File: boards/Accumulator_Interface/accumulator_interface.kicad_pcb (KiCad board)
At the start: 2 copper layers, 0 parts

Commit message: added traces to accumulator
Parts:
- added J1: INTERNAL, footprints:Ultrafit_4, B.Cu at (64.5, 64.0)
- added J10: AIR_CTRL_18, footprints:micromatch_female_vert_18, B.Cu at (37.8, 54.6)
- added J2: EXTERNAL, footprints:Ampseal_35, F.Cu at (115.3, 44.2)
- added J3: AIR_CTRL, footprints:Ultrafit_2, B.Cu at (113.3, 66.3)
- added J4: IMD_LATCH, footprints:Ultrafit_2, B.Cu at (102.9, 66.3)
- added J5: DISCHARGE, footprints:Ultrafit_2, B.Cu at (91.9, 66.3)
- added J6: BMS_Master, footprints:Ultrafit_4, B.Cu at (80.8, 64.0)
- added J7: BMS, footprints:micromatch_female_vert_12, B.Cu at (47.8, 85.9)
- added J8: TSAL/AIL, footprints:micromatch_female_vert_4, B.Cu at (45.7, 36.8)
- added J9: IMD_LATCH, footprints:micromatch_female_vert_4, B.Cu at (45.7, 50.0)
- added U1: RJ45_VT_AIR, footprints:RJ45-Vertical, F.Cu at (52.1, 67.8)
- added U2: RJ45_VT_BMS, footprints:RJ45-Vertical, F.Cu at (38.9, 100.3)
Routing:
- net /CAN_LOW: track 0.00 -> 194.2 mm
- net /BMS_IN/IMD_LATCH_OUT: track 0.00 -> 79.7 mm
- net /IMD_LATCH_IN/HVD_OUT: track 0.00 -> 74.1 mm
- net /CAN_HIGH: track 0.00 -> 46.5 mm, vias 0 -> 1
- net /HVD_IN/MAIN_PACK_OUT: track 0.00 -> 44.3 mm
- net /TSAL+: track 0.00 -> 27.1 mm
- net /SCK_AIR: track 0.00 -> 26.0 mm
- net /TSMS_IN: track 0.00 -> 24.3 mm
- net /MISO_AIR: track 0.00 -> 23.1 mm, vias 0 -> 1
- net /MOSI_AIR: track 0.00 -> 22.4 mm
- net /AIR_CTRL_LED_1: track 0.00 -> 21.1 mm
- net /AIR_CTRL_5V_OUT: track 0.00 -> 20.2 mm
- net /BMS_LED_2: track 0.00 -> 17.8 mm, vias 0 -> 1
- net /TSAL-: track 0.00 -> 17.6 mm
- net /IMD_LATCH_STATUS: track 0.00 -> 16.9 mm, vias 0 -> 2
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
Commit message: Accu Interface updates
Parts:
- added J11: Energy_Meter_Power, footprints:Ultrafit_2, B.Cu at (66.2, 77.0)
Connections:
- J10 pad 12: /BMS_IN/IMD_LATCH_OUT -> /BMS_STATUS
- J10 pad 13: /IMD_LATCH_IN/HVD_OUT -> /IMD_LATCH_STATUS
- J10 pad 14: /MAIN_PACK_IN/BMS_OUT -> /BMS_IN/IMD_LATCH_OUT
- J10 pad 15: /HVD_IN/MAIN_PACK_OUT -> /IMD_LATCH_IN/HVD_OUT
- J10 pad 16: /BMS_STATUS -> /MAIN_PACK_IN/BMS_OUT
- J10 pad 17: /IMD_LATCH_STATUS -> /HVD_IN/MAIN_PACK_OUT
- J10 pad 18: Net-(J10-Pad18) -> (no net)
- J2 pad 16: Net-(J2-Pad16) -> (no net)
- J2 pad 17: Net-(J2-Pad17) -> (no net)
- J2 pad 18: Net-(J2-Pad18) -> (no net)
- J2 pad 19: Net-(J2-Pad19) -> (no net)
- J2 pad 20: Net-(J2-Pad20) -> (no net)
- J2 pad 21: Net-(J2-Pad21) -> (no net)
- J2 pad 22: Net-(J2-Pad22) -> (no net)
- J2 pad 23: Net-(J2-Pad23) -> (no net)
- J2 pad 33: Net-(J2-Pad33) -> (no net)
- J3 pad 2: Net-(J3-Pad2) -> (no net)
- U1 pad 3: Net-(U1-Pad3) -> /AIR_CTRL_RESET
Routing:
- net /12V: track 0.00 -> 153.2 mm, vias 0 -> 8
- net /CAN_HIGH: track 46.5 -> 136.9 mm, vias 1 -> 3
- net /BSPD_CURRENT_SENSE: track 0.00 -> 84.3 mm, vias 0 -> 9
- net /CAN_LOW: track 194.2 -> 122.8 mm, vias 0 -> 4
- net /FAN_PWM: track 0.00 -> 62.6 mm, vias 0 -> 6
- net /BMS_STATUS: track 0.00 -> 46.2 mm, vias 0 -> 3
- net /CRASH_IN/HVD_OUT: track 11.0 -> 54.7 mm
- net /MAIN_PACK_IN/BMS_OUT: track 15.5 -> 56.5 mm, vias 0 -> 1
- net /AIR_CTRL_LED_2: track 0.00 -> 40.3 mm, vias 0 -> 1
- net /TSMS_IN: track 24.3 -> 62.0 mm, vias 0 -> 2
- net /BMS_LED_1: track 0.00 -> 29.3 mm, vias 0 -> 1
- net /AIR_CTRL_RESET: track 0.00 -> 27.1 mm, vias 0 -> 2
- net /GND: track 0.00 -> 8.00 mm
- net /FAN_GND: track 0.00 -> 8.00 mm
- net /FAN_12V: track 0.00 -> 8.00 mm
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- added copper zone on B.Cu, net /GND
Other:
- board text added: "12V"
- board text added: "BMS_OUT"
- board text added: "HVD_OUT"
- board text added: "IMD_LATCH_OUT"
- board text added: "MAIN_PACK_OUT"
- board text added: "TSMS_IN"

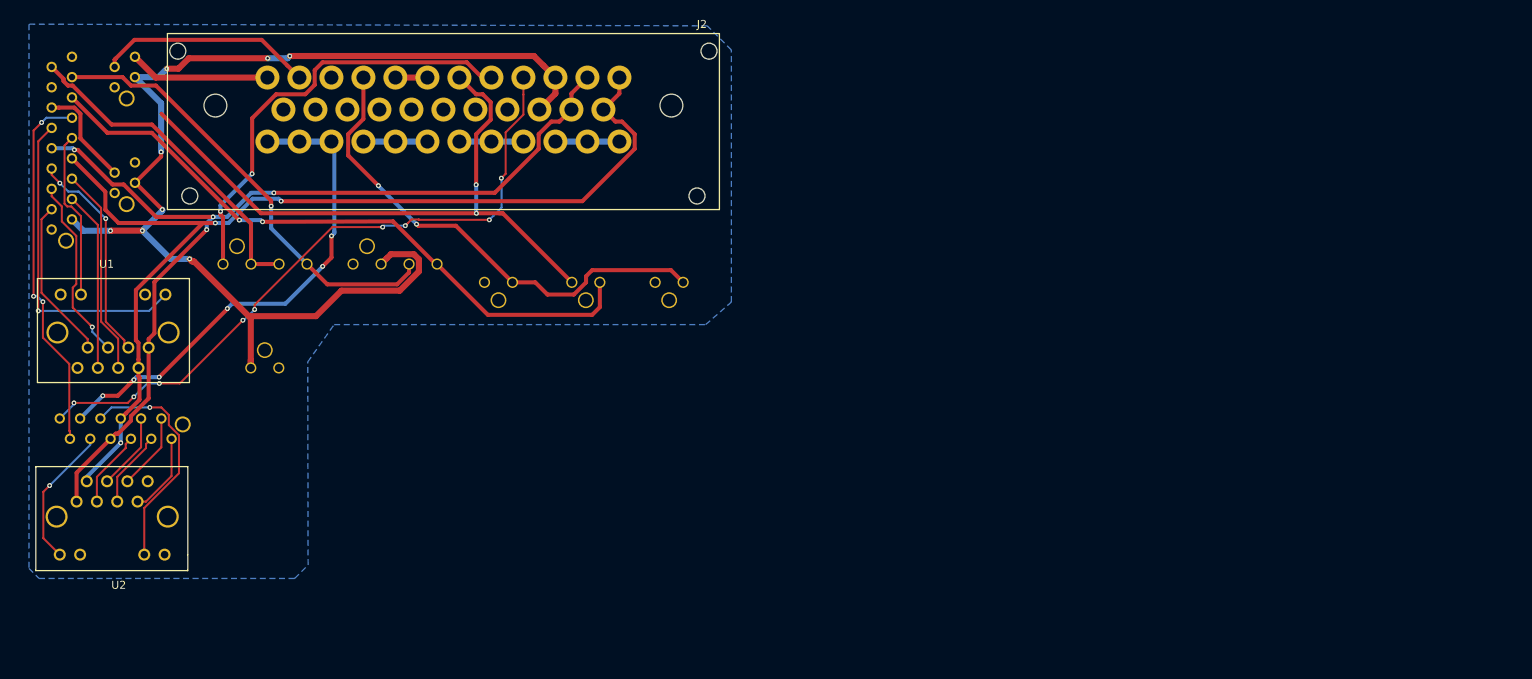
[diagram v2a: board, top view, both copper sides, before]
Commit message: Modified layout for accumulator board.
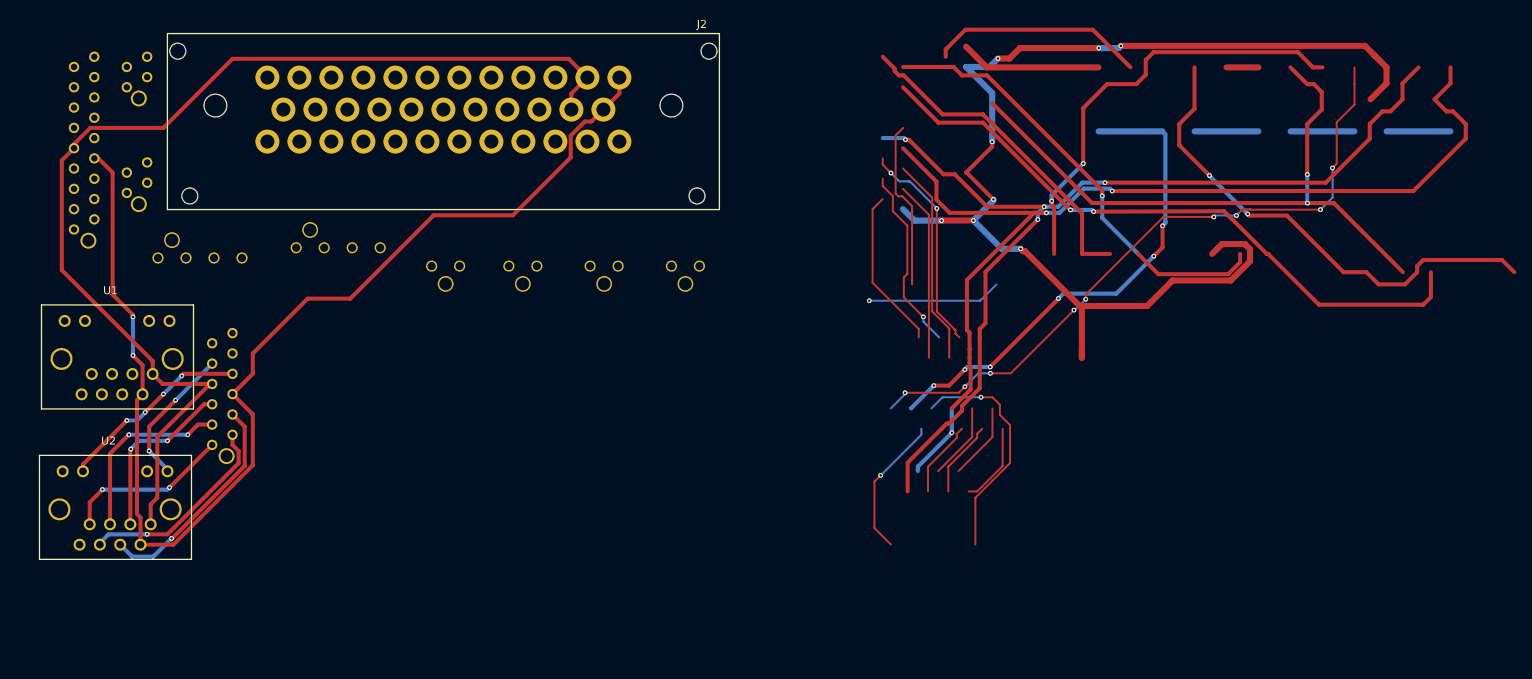
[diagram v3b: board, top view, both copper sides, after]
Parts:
- moved J11 31.4 mm to (95.0, 64.3), turned to 270 degrees
- moved U2 17.0 mm to (52.3, 89.9), turned to 180 degrees
- moved J7 11.0 mm to (57.9, 81.5), turned to 0 degrees
- moved J1 8.16 mm to (56.4, 63.2)
- moved J6 7.40 mm to (73.7, 62.0)
- moved J5 6.91 mm to (85.3, 64.3)
- moved U1 3.34 mm to (52.6, 71.1)
- moved J4 3.06 mm to (105.2, 64.3)
- moved J3 2.87 mm to (115.3, 64.3)
- moved J10 2.79 mm to (40.6, 54.6)
- moved J8 1.52 mm to (47.2, 36.8)
- moved J9 1.52 mm to (47.2, 50.0)
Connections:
- J10 pad 12: /BMS_STATUS -> /IMD_LATCH_STATUS
- J10 pad 13: /IMD_LATCH_STATUS -> /BMS_STATUS
- J10 pad 18: (no net) -> Net-(J10-Pad18)
- J2 pad 16: (no net) -> Net-(J2-Pad16)
- J2 pad 17: (no net) -> Net-(J2-Pad17)
- J2 pad 18: (no net) -> Net-(J2-Pad18)
- J2 pad 19: (no net) -> Net-(J2-Pad19)
- J2 pad 20: (no net) -> Net-(J2-Pad20)
- J2 pad 21: (no net) -> Net-(J2-Pad21)
- J2 pad 22: (no net) -> Net-(J2-Pad22)
- J2 pad 23: (no net) -> Net-(J2-Pad23)
- J2 pad 33: (no net) -> Net-(J2-Pad33)
- J3 pad 2: (no net) -> Net-(J3-Pad2)
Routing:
- net (no net): track 0.00 -> 1261.2 mm, vias 0 -> 45
- net /12V: track 153.2 -> 0.00 mm, vias 8 -> 0
- net /BSPD_CURRENT_SENSE: track 84.3 -> 0.00 mm, vias 9 -> 0
- net /BMS_IN/IMD_LATCH_OUT: track 80.8 -> 0.00 mm, vias 2 -> 0
- net /IMD_LATCH_IN/HVD_OUT: track 80.3 -> 0.00 mm, vias 2 -> 0
- net /FAN_PWM: track 62.6 -> 0.00 mm, vias 6 -> 0
- net /TSMS_IN: track 62.0 -> 0.00 mm, vias 2 -> 0
- net /MAIN_PACK_IN/BMS_OUT: track 56.5 -> 0.00 mm, vias 1 -> 0
- net /CRASH_IN/HVD_OUT: track 54.7 -> 0.00 mm, vias 2 -> 0
- net /BMS_STATUS: track 46.2 -> 0.00 mm, vias 3 -> 0
- net /HVD_IN/MAIN_PACK_OUT: track 41.8 -> 0.00 mm
- net /AIR_CTRL_LED_2: track 40.3 -> 0.00 mm, vias 1 -> 0
- net /TSAL+: track 27.2 -> 0.00 mm
- net /AIR_CTRL_RESET: track 27.1 -> 0.00 mm, vias 2 -> 0
- net /SCK_AIR: track 26.0 -> 0.00 mm
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- removed copper zone on B.Cu, net /GND

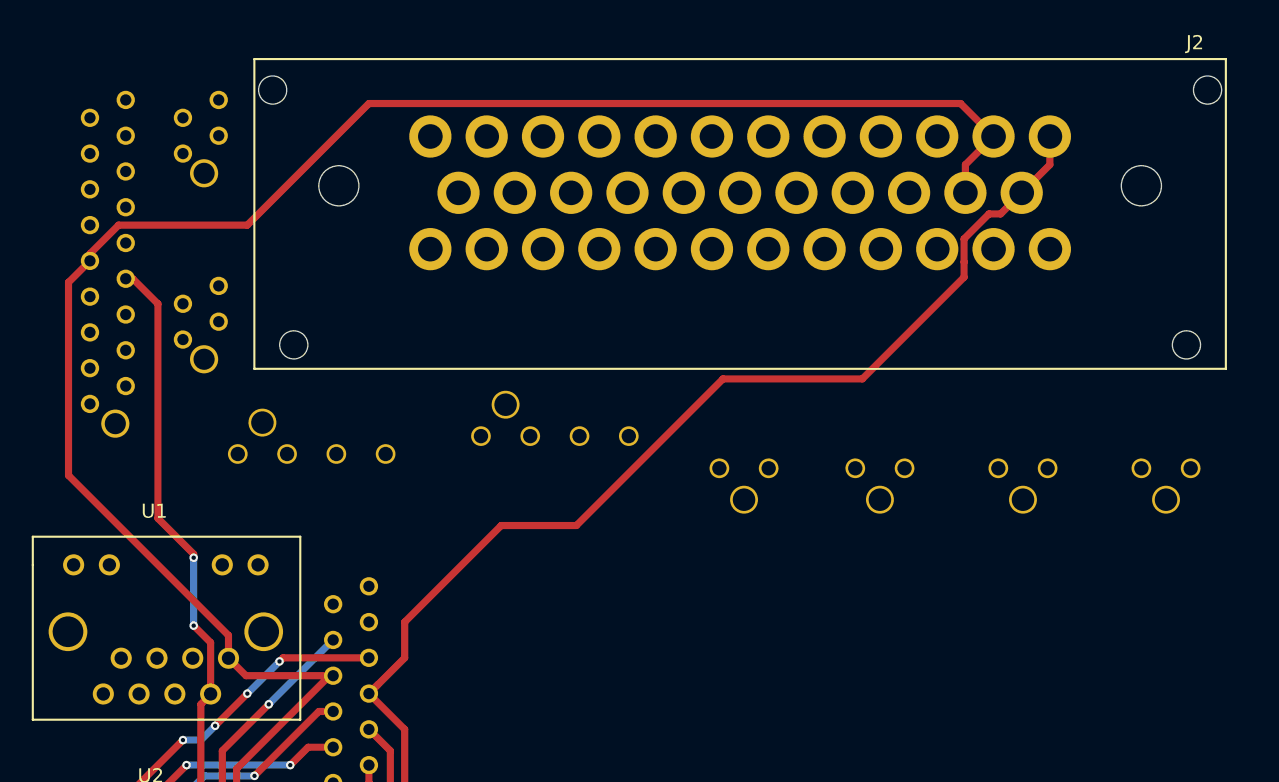
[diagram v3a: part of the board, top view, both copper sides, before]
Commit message: added more traces
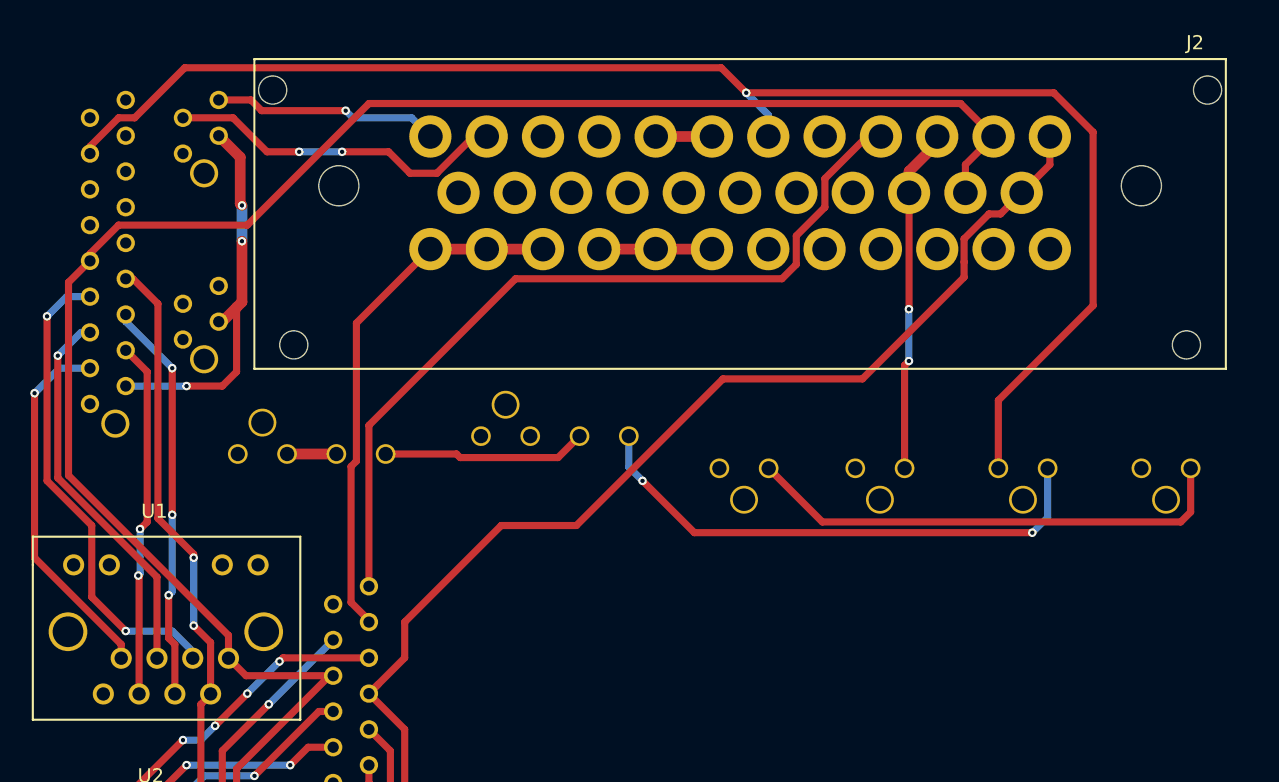
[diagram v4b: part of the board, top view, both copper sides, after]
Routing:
- net /IMD_LATCH_IN/HVD_OUT: track 0.00 -> 106.4 mm, vias 0 -> 1
- net /BSPD_CURRENT_SENSE: track 0.00 -> 58.7 mm
- net /12V: track 0.00 -> 52.1 mm, vias 0 -> 5
- net /BMS_IN/IMD_LATCH_OUT: track 0.00 -> 37.8 mm, vias 0 -> 2
- net /FAN_PWM: track 0.00 -> 37.3 mm
- net /TSMS_IN: track 0.00 -> 34.9 mm
- net /AIR_CTRL_RESET: track 0.00 -> 34.1 mm, vias 0 -> 2
- net /SCK_AIR: track 0.00 -> 28.6 mm, vias 0 -> 3
- net /MISO_AIR: track 0.00 -> 27.4 mm, vias 0 -> 1
- net /AIR_CTRL_5V_OUT: track 0.00 -> 26.0 mm, vias 0 -> 1
- net /TSAL+: track 0.00 -> 25.8 mm, vias 0 -> 2
- net /MOSI_AIR: track 0.00 -> 25.3 mm, vias 0 -> 2
- net /TSAL-: track 0.00 -> 16.1 mm, vias 0 -> 1
- net /MAIN_PACK_IN/BMS_OUT: track 0.00 -> 14.5 mm
- net /FAN_12V: track 0.00 -> 8.00 mm
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
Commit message: Accum Update
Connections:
- J10 pad 18: Net-(J10-Pad18) -> (no net)
- J2 pad 16: Net-(J2-Pad16) -> /12V
- J2 pad 17: Net-(J2-Pad17) -> /12V
- J2 pad 18: Net-(J2-Pad18) -> /CAN_LOW
- J2 pad 19: Net-(J2-Pad19) -> /CAN_LOW
- J2 pad 20: Net-(J2-Pad20) -> /CAN_HIGH
- J2 pad 21: Net-(J2-Pad21) -> /CAN_HIGH
- J2 pad 22: Net-(J2-Pad22) -> /GND
- J2 pad 23: Net-(J2-Pad23) -> /GND
- J2 pad 33: Net-(J2-Pad33) -> (no net)
- J2 pad 4: /FAN_GND -> /GND
- J2 pad 5: /FAN_GND -> /GND
- J2 pad 6: /FAN_GND -> /GND
- J2 pad 7: /FAN_12V -> /12V
- J2 pad 8: /FAN_12V -> /12V
- J2 pad 9: /FAN_12V -> /12V
- J3 pad 2: Net-(J3-Pad2) -> (no net)
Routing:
- net /12V: track 52.1 -> 162.7 mm, vias 5 -> 10
- net /CAN_HIGH: track 149.9 -> 219.0 mm, vias 2 -> 4
- net /CRASH_IN/HVD_OUT: track 0.00 -> 62.0 mm, vias 0 -> 5
- net /BMS_IN/IMD_LATCH_OUT: track 37.8 -> 82.8 mm, vias 2 -> 8
- net /HVD_IN/MAIN_PACK_OUT: track 3.50 -> 48.5 mm, vias 0 -> 4
- net /BMS_STATUS: track 0.00 -> 37.4 mm, vias 0 -> 2
- net /MAIN_PACK_IN/BMS_OUT: track 14.5 -> 47.0 mm, vias 0 -> 3
- net /AIR_CTRL_LED_2: track 0.00 -> 30.1 mm, vias 0 -> 3
- net /TSMS_IN: track 34.9 -> 64.6 mm, vias 0 -> 4
- net /AIR_CTRL_LED_1: track 0.00 -> 25.1 mm, vias 0 -> 1
- net /GND: track 0.00 -> 24.0 mm
- net /CAN_LOW: track 137.3 -> 154.5 mm, vias 0 -> 1
- net /IMD_LATCH_STATUS: track 0.00 -> 9.43 mm, vias 0 -> 1
- net /FAN_12V: track 8.00 -> 0.00 mm
- net /SCK_AIR: track 28.6 -> 30.3 mm, vias 3 -> 4
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- added copper zone on B.Cu, net /GND

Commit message: Accum Update
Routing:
- net /CAN_HIGH: track 219.0 -> 221.2 mm
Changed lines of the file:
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@@
   (general
     (links 83)
-    (no_connects 8)
+    (no_connects 0)
     (area 19.692111 25.50813 221.076402 105.306801)
     (thickness 1.6)
     (drawings 20)
-    (tracks 895)
+    (tracks 900)
     (zones 0)
     (modules 13)
@@
   )
   (setup
-    (last_trace_width 0.508)
+    (last_trace_width 0.762)
     (user_trace_width 0.254)
     (user_trace_width 0.508)
@@
   (segment (start 46.228 76.327) (end 46.228 73.279) (width 0.508) (layer F.Cu) (net 16))
   (segment (start 46.668 76.767) (end 46.228 76.327) (width 0.508) (layer F.Cu) (net 16))
-  (segment (start 78.816 44.696) (end 80.315999 46.195999) (width 0.508) (layer B.Cu) (net 17))
-  (segment (start 82.909599 47.968125) (end 82.909599 50.736923) (width 0.508) (layer B.Cu) (net 17))
-  (segment (start 80.315999 46.195999) (end 81.137473 46.195999) (width 0.508) (layer B.Cu) (net 17))
-  (segment (start 82.909599 50.736923) (end 87.595468 55.422792) (width 0.508) (layer B.Cu) (net 17))
-  (segment (start 81.137473 46.195999) (end 82.909599 47.968125) (width 0.508) (layer B.Cu) (net 17))
-  (segment (start 87.595468 55.422792) (end 87.900267 55.727591) (width 0.508) (layer B.Cu) (net 17))
-  (segment (start 74.816 44.696) (end 74.816 50.433054) (width 0.508) (layer B.Cu) (net 17))
-  (segment (start 74.816 50.433054) (end 80.110537 55.727591) (width 0.508) (layer B.Cu) (net 17))
-  (segment (start 80.110537 55.727591) (end 87.469215 55.727591) (width 0.508) (layer B.Cu) (net 17))
-  (segment (start 87.469215 55.727591) (end 87.900267 55.727591) (width 0.508) (layer B.Cu) (net 17))
+  (segment (start 74.816 47.92472) (end 74.816 49.75352) (width 0.508) (layer B.Cu) (net 17))
+  (segment (start 74.816 44.696) (end 74.816 47.92472) (width 0.762) (layer B.Cu) (net 17))
+  (segment (start 74.816 49.75352) (end 74.816 50.61266) (width 0.762) (layer B.Cu) (net 17))
+  (segment (start 74.816 50.61266) (end 79.930931 55.727591) (width 0.762) (layer B.Cu) (net 17))
+  (segment (start 87.469215 55.727591) (end 87.900267 55.727591) (width 0.762) (layer B.Cu) (net 17))
+  (segment (start 79.930931 55.727591) (end 87.469215 55.727591) (width 0.762) (layer B.Cu) (net 17))
+  (segment (start 82.849401 47.719967) (end 82.849401 49.672033) (width 0.508) (layer B.Cu) (net 17))
+  (segment (start 82.849401 49.672033) (end 82.782599 49.738835) (width 0.508) (layer B.Cu) (net 17))
+  (segment (start 82.849401 47.907927) (end 82.849401 47.719967) (width 0.762) (layer B.Cu) (net 17))
+  (segment (start 82.849401 47.719967) (end 81.325433 46.195999) (width 0.762) (layer B.Cu) (net 17))
+  (segment (start 81.325433 46.195999) (end 80.315999 46.195999) (width 0.762) (layer B.Cu) (net 17))
+  (segment (start 80.315999 46.195999) (end 78.816 44.696) (width 0.762) (layer B.Cu) (net 17))
+  (segment (start 82.909599 47.968125) (end 82.782599 49.738835) (width 0.508) (layer B.Cu) (net 17))
+  (segment (start 87.900267 55.727591) (end 82.782599 50.609923) (width 0.762) (layer B.Cu) (net 17))
+  (segment (start 82.782599 50.609923) (end 82.782599 49.738835) (width 0.762) (layer B.Cu) (net 17))
   (via (at 87.900267 55.727591) (size 0.6096) (drill 0.3048) (layers F.Cu B.Cu) (net 17))
   (segment (start 78.816 44.696) (end 74.816 44.696) (width 0.762) (layer B.Cu) (net 17))
